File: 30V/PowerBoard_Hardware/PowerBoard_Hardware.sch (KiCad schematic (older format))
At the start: 131 parts, among them Q1 Q_NMOS_GDS, Q10 Q_NMOS_GDS, Q2 Q_NMOS_GDS, Q3 Q_NMOS_GDS, Q4 Q_NMOS_GDS, Q5 Q_NMOS_GDS, Q6 Q_NMOS_GDS, Q7 Q_NMOS_GDS, Q8 Q_NMOS_GDS, Q9 Q_NMOS_GDS, U1 LT1910, U10 LT1910, U11 LT1910, U12 ACS722xLCTR-40AU, U13 ACS722xLCTR-40AU, U14 ACS722xLCTR-40AU, U15 OKI_5V, U16 OKI_3V3, U17 LT1910, U18 LT1910, U19 ACS722xLCTR-40AU, U2 LT1910, U20 ACS722xLCTR-40AU, U21 LT1910, U22 ACS722xLCTR-40AU, U3 LT1910, U4 LT1910, U5 ACS722xLCTR-40AU, U6 ACS722xLCTR-40AU, U7 ACS722xLCTR-40AU, U8 ACS722xLCTR-40AU, U9 LT1910

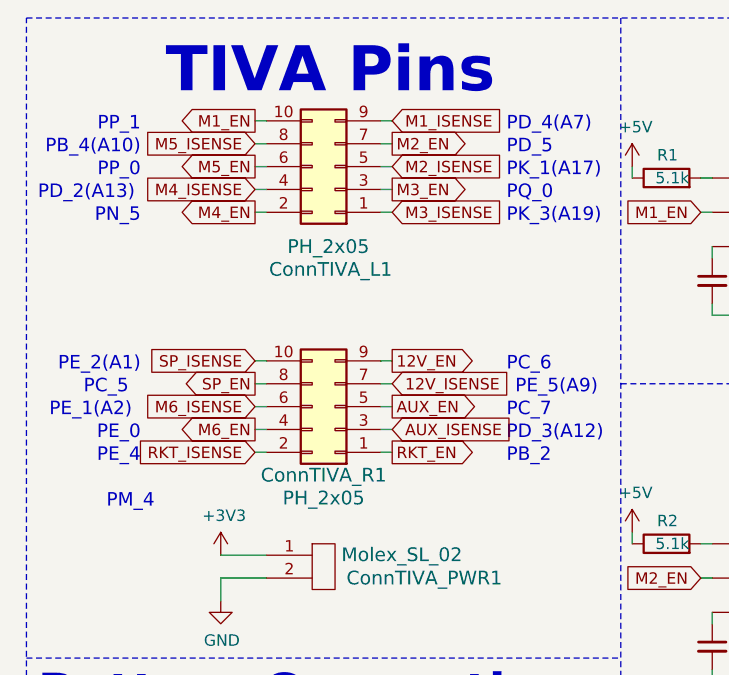
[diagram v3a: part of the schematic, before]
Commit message: Finished Rev 2, minus potential grounding via
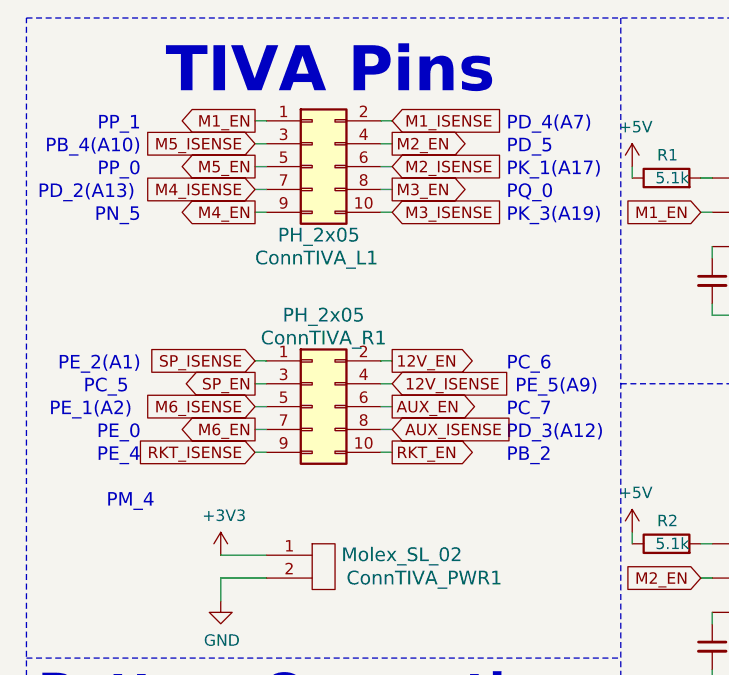
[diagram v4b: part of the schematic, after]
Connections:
- net 12V_EN: now also ConnTIVA_R1.2 (Pin_2); no longer ConnTIVA_R1.9 (Pin_9)
- net 12V_ISENSE: now also ConnTIVA_R1.4 (Pin_4); no longer ConnTIVA_R1.7 (Pin_7)
- net AUX_EN: now also ConnTIVA_R1.6 (Pin_6); no longer ConnTIVA_R1.5 (Pin_5)
- net AUX_ISENSE: now also ConnTIVA_R1.8 (Pin_8); no longer ConnTIVA_R1.3 (Pin_3)
- net M1_EN: now also ConnTIVA_L1.1 (Pin_1); no longer ConnTIVA_L1.10 (Pin_10)
- net M1_ISENSE: now also ConnTIVA_L1.2 (Pin_2); no longer ConnTIVA_L1.9 (Pin_9)
- net M2_EN: now also ConnTIVA_L1.4 (Pin_4); no longer ConnTIVA_L1.7 (Pin_7)
- net M2_ISENSE: now also ConnTIVA_L1.6 (Pin_6); no longer ConnTIVA_L1.5 (Pin_5)
- net M3_EN: now also ConnTIVA_L1.8 (Pin_8); no longer ConnTIVA_L1.3 (Pin_3)
- net M3_ISENSE: now also ConnTIVA_L1.10 (Pin_10); no longer ConnTIVA_L1.1 (Pin_1)
- net M4_EN: now also ConnTIVA_L1.9 (Pin_9); no longer ConnTIVA_L1.2 (Pin_2)
- net M4_ISENSE: now also ConnTIVA_L1.7 (Pin_7); no longer ConnTIVA_L1.4 (Pin_4)
- net M5_EN: now also ConnTIVA_L1.5 (Pin_5); no longer ConnTIVA_L1.6 (Pin_6)
- net M5_ISENSE: now also ConnTIVA_L1.3 (Pin_3); no longer ConnTIVA_L1.8 (Pin_8)
- net M6_EN: now also ConnTIVA_R1.7 (Pin_7); no longer ConnTIVA_R1.4 (Pin_4)
- net M6_ISENSE: now also ConnTIVA_R1.5 (Pin_5); no longer ConnTIVA_R1.6 (Pin_6)
- net RKT_EN: now also ConnTIVA_R1.10 (Pin_10); no longer ConnTIVA_R1.1 (Pin_1)
- net RKT_ISENSE: now also ConnTIVA_R1.9 (Pin_9); no longer ConnTIVA_R1.2 (Pin_2)
- net SP_EN: now also ConnTIVA_R1.3 (Pin_3); no longer ConnTIVA_R1.8 (Pin_8)
- net SP_ISENSE: now also ConnTIVA_R1.1 (Pin_1); no longer ConnTIVA_R1.10 (Pin_10)
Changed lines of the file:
@@
 L Connector_Generic:Conn_02x05_Odd_Even ConnTIVA_L1
 U 1 1 5DD2C1C3
-P 1800 1100
-F 0 "ConnTIVA_L1" H 1550 1550 60  0000 L CNN
-F 1 "PH_2x05" H 1650 1450 60  0000 L CNN
-F 2 "MRDT_Connectors:JTAG_ARM_Connector_10_Pin" H 1800 1400 60  0001 C CNN
-F 3 "" H 1800 1400 60  0001 C CNN
-	1    1800 1100
-	-1   0    0    1
+P 1700 1100
+F 0 "ConnTIVA_L1" H 1450 700 60  0000 L CNN
+F 1 "PH_2x05" H 1550 800 60  0000 L CNN
+F 2 "MRDT_Connectors:JTAG_ARM_Connector_10_Pin" H 1700 1400 60  0001 C CNN
+F 3 "" H 1700 1400 60  0001 C CNN
+	1    1700 1100
+	1    0    0    -1
 $EndComp
 $Comp
@@
 L Connector_Generic:Conn_02x05_Odd_Even ConnTIVA_R1
 U 1 1 5DD2EFB6
-P 1800 2150
-F 0 "ConnTIVA_R1" H 1850 2450 60  0000 C CNN
-F 1 "PH_2x05" H 1850 2550 60  0000 C CNN
-F 2 "MRDT_Connectors:JTAG_ARM_Connector_10_Pin" H 1800 2450 60  0001 C CNN
-F 3 "" H 1800 2450 60  0001 C CNN
-	1    1800 2150
-	-1   0    0    1
+P 1700 2150
+F 0 "ConnTIVA_R1" H 1750 2450 60  0000 C CNN
+F 1 "PH_2x05" H 1750 2550 60  0000 C CNN
+F 2 "MRDT_Connectors:JTAG_ARM_Connector_10_Pin" H 1700 2450 60  0001 C CNN
+F 3 "" H 1700 2450 60  0001 C CNN
+	1    1700 2150
+	1    0    0    -1
 $EndComp
 Text Notes 2950 2100 2    59   ~ 0

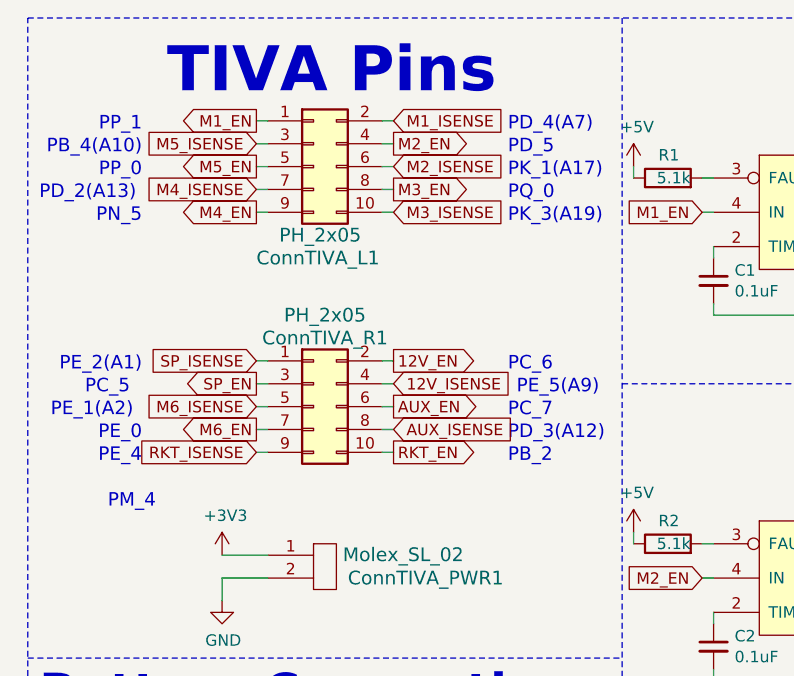
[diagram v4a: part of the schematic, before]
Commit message: Ready for Rev 2 review, minus frame ground
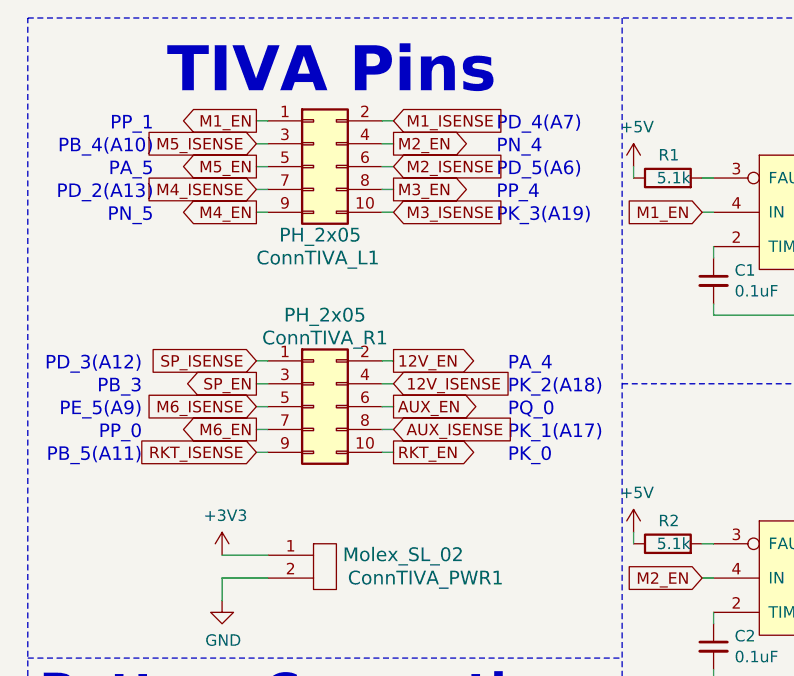
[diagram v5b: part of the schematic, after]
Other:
- note added: "PA_4"
- note added: "PA_5"
- note added: "PB_3"
- note added: "PB_5(A11)"
- note added: "PD_5(A6)"
- note added: "PK_0"
- note added: "PK_2(A18)"
- note added: "PN_4"
- note added: "PP_4"
- note removed: "PB_2"
- note removed: "PC_5"
- note removed: "PC_6"
- note removed: "PC_7"
- note removed: "PD_5"
- note removed: "PE_0"
- note removed: "PE_1(A2)"
- note removed: "PE_2(A1)"
- note removed: "PE_4"
- note removed: "PM_4"
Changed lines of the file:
@@
 Text Notes 5100 4050 0    157  ~ 31
 Motor3
-Text Notes 800  2600 0    59   ~ 0
-PM_4
-Text Notes 950  2300 2    59   ~ 0
-PE_0
-Text Notes 700  2100 0    59   ~ 0
-PC_5
-Text Notes 2550 2000 0    59   ~ 0
-PC_6
-Text Notes 2550 2200 0    59   ~ 0
-PC_7
-Text Notes 950  2000 2    59   ~ 0
-PE_2(A1)
-Text Notes 950  2400 2    59   ~ 0
-PE_4
-Text Notes 550  2200 0    59   ~ 0
-PE_1(A2)
-Text Notes 950  1050 2    59   ~ 0
+Text Notes 1000 1050 2    59   ~ 0
 PB_4(A10)
-Text Notes 2550 1150 0    59   ~ 0
+Text Notes 2550 2300 0    59   ~ 0
 PK_1(A17)
-Text Notes 500  1250 0    59   ~ 0
+Text Notes 1000 1250 2    59   ~ 0
 PD_2(A13)
-Text Notes 2550 1050 0    59   ~ 0
-PD_5
+Text Notes 1000 1150 2    59   ~ 0
+PA_5
 Wire Wire Line
 	1500 2350 1450 2350
@@
 Wire Wire Line
 	2050 2350 2000 2350
-Text Notes 2550 2300 0    59   ~ 0
+Text Notes 950  2000 2    59   ~ 0
 PD_3(A12)
-Text Notes 2550 2400 0    59   ~ 0
-PB_2
+Text Notes 950  2100 2    59   ~ 0
+PB_3
 Text GLabel 1450 1200 0    50   Input ~ 0
 M4_ISENSE
@@
 Wire Wire Line
 	1450 1000 1500 1000
-Text Notes 2550 1250 0    59   ~ 0
+Text Notes 2550 2200 0    59   ~ 0
 PQ_0
-Text Notes 950  1350 2    59   ~ 0
+Text Notes 1000 1350 2    59   ~ 0
 PN_5
-Text Notes 950  1150 2    59   ~ 0
+Text Notes 950  2300 2    59   ~ 0
 PP_0
-Text Notes 950  950  2    59   ~ 0
+Text Notes 1000 950  2    59   ~ 0
 PP_1
 Wire Wire Line
@@
 	1    0    0    -1
 $EndComp
-Text Notes 2950 2100 2    59   ~ 0
+Text Notes 950  2200 2    59   ~ 0
 PE_5(A9)
-Text Notes 2550 1350 0    59   ~ 0
-PK_3(A19)
-Text Notes 2550 950  0    59   ~ 0
+Text Notes 2550 2100 0    59   ~ 0
+PK_2(A18)
+Text Notes 2500 950  0    59   ~ 0
 PD_4(A7)
 Wire Notes Line
@@
 	1    0    0    -1
 $EndComp
+Text Notes 950  2400 2    59   ~ 0
+PB_5(A11)
+Text Notes 2550 2400 0    59   ~ 0
+PK_0
+Text Notes 2550 2000 0    59   ~ 0
+PA_4
+Text Notes 2500 1150 0    59   ~ 0
+PD_5(A6)
+Text Notes 2500 1250 0    59   ~ 0
+PP_4
+Text Notes 2500 1050 0    59   ~ 0
+PN_4
+Text Notes 2500 1350 0    59   ~ 0
+PK_3(A19)
 $EndSCHEMATC
